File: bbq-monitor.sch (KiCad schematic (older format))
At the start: 51 parts, among them J1 Power, J2 USB_B_Mini, J3 Thermocouple, Q1 AO3401A, Q2 BC847, Q3 BC847, SW1 SW_Push, U1 ESP32-WROOM-32D, U2 TPS62132, U3 CP2104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

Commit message: up
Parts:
- removed C12, C14: 100n, Capacitor_SMD:C_0603_1608Metric, symbol Device:C_Small
- removed C13, C15: 10n, Capacitor_SMD:C_0603_1608Metric, symbol Device:C_Small
- removed C16: 100n, Capacitor_SMD:C_0402_1005Metric, symbol Device:C_Small
- removed C17: 10u, Capacitor_SMD:C_0402_1005Metric, symbol Device:C_Small
- removed H4: TR, MountingHole:MountingHole_3.2mm_M3_Pad_Via, symbol Mechanical:MountingHole
- removed U5: AD8495, Package_SO:MSOP-8_3x3mm_P0.65mm, symbol Sensor_Temperature:AD8495
- removed U6: DHT11, Sensor:Aosong_DHT11_5.5x12.0_P2.54mm, symbol Sensor:DHT11
- added C9: 100n, Capacitor_SMD:C_0603_1608Metric, symbol Device:C_Small
- added D3, D4, D5: RED, LED_SMD:LED_0603_1608Metric, symbol Device:LED_Small
- added D6: D_Zener, Diode_SMD:D_1206_3216Metric, symbol Device:D_Zener
- added D7: D_Schottky, Diode_SMD:D_1206_3216Metric, symbol Device:D_Schottky
- added IC1: MAX6675, hardware libraries:SO08, symbol MAX6675:MAX6675
- added Q4: AO3401A, Package_TO_SOT_SMD:SOT-23, symbol Transistor_FET:AO3401A
- J1: value Power -> Battery Power
- R10, R11, R9: value 1M -> 220; LCSC Part # C4190 -> (none)
- R13: value 100 -> 10k
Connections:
- net +3V3: now also C9.1, D3.2 (A), D4.2 (A), D5.2 (A), IC1.4 (VCC); no longer R12.1
- net +5V: now also R12.2, D7.2 (A), Q4.1 (G)
- net GND: now also J3.1 (Pin_1), R12.1, C9.2, IC1.1 (GND), IC1.2 (T-)
- net THERMO_SPI_CS: now reaches U1.29 (IO5)
- net THERMO_SPI_CS: now also IC1.6 (/CS)
- net THERMO_SPI_CLK: now reaches U1.30 (IO18)
- net THERMO_SPI_CLK: now also IC1.5 (SCK)
- net THERMO_SPI_DO: now reaches U1.31 (IO19)
- net THERMO_SPI_DO: now also IC1.7 (DO)
- net RX_LED: now reaches U3.13 (GPIO.1)
- net RX_LED: now also R11.1
- net TX_LED: now reaches U3.14 (GPIO.0)
- net TX_LED: now also R10.1
- net BATT_PWR: now reaches F1.2, J1.1 (Pin_1)
- net at Q1.1 (G), R13.2: now also D6.2 (A)
- net at J3.2 (Pin_2): now also IC1.3 (T+); no longer R10.1
- net BATT: no longer names the net of C1.1, C2.1, U2.10 (AVIN), U2.11 (PVIN), U2.12 (PVIN), U2.13 (EN)
- net BATT: now also D7.1 (K), Q4.2 (S); no longer Q1.2 (S), R14.1
- net TEMP_HUMID_SEN: no longer names the net of U1.6 (IO34)
- net TEMP_HUMID_SEN: no longer R12.2
- net THERMOCOUPLE: no longer names the net of U1.11 (IO26)
- net Thermocouple_INPUT_FILTERED+: no longer names the net of R10.2
- net Thermocouple_INPUT_FILTERED+: now also D4.1 (K)
- net Thermocouple_INPUT_FILTERED-: no longer names the net of R11.2
- net Thermocouple_INPUT_FILTERED-: now also D5.1 (K)
- new net: D3.1 (K), R9.2
- new net BATT_SAFE: D6.1 (K), Q1.2 (S), Q4.3 (D), R14.1
- no-connect marks 38 -> 35
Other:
- note added: "15V"
- note added: "LEDs\n"
- note added: "Schottky Value at Max Input Voltage"
- note added: "T+\n"
- note added: "T-\n"
- note removed: "Temperature and Humidity\n"
- moved on the sheet: C1, C10, C11, C2, C3, C4, C5, C6, C7, C8, D1, D2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

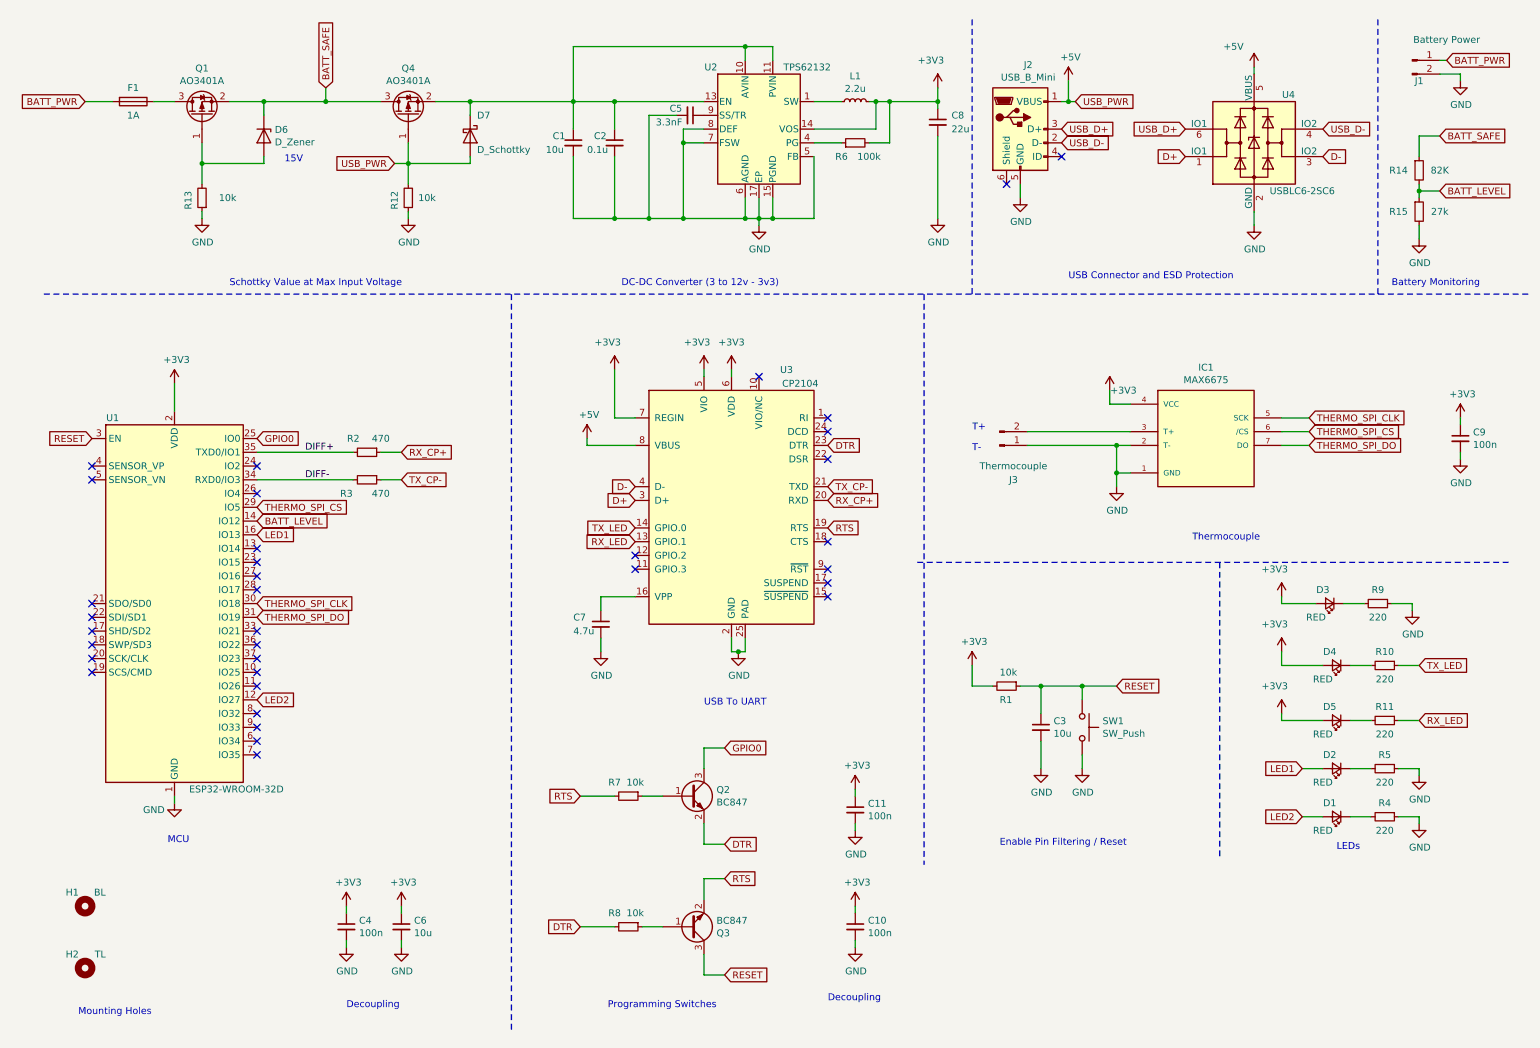
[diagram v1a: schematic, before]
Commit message: dc-dc is too expexpesnive - project is on hold
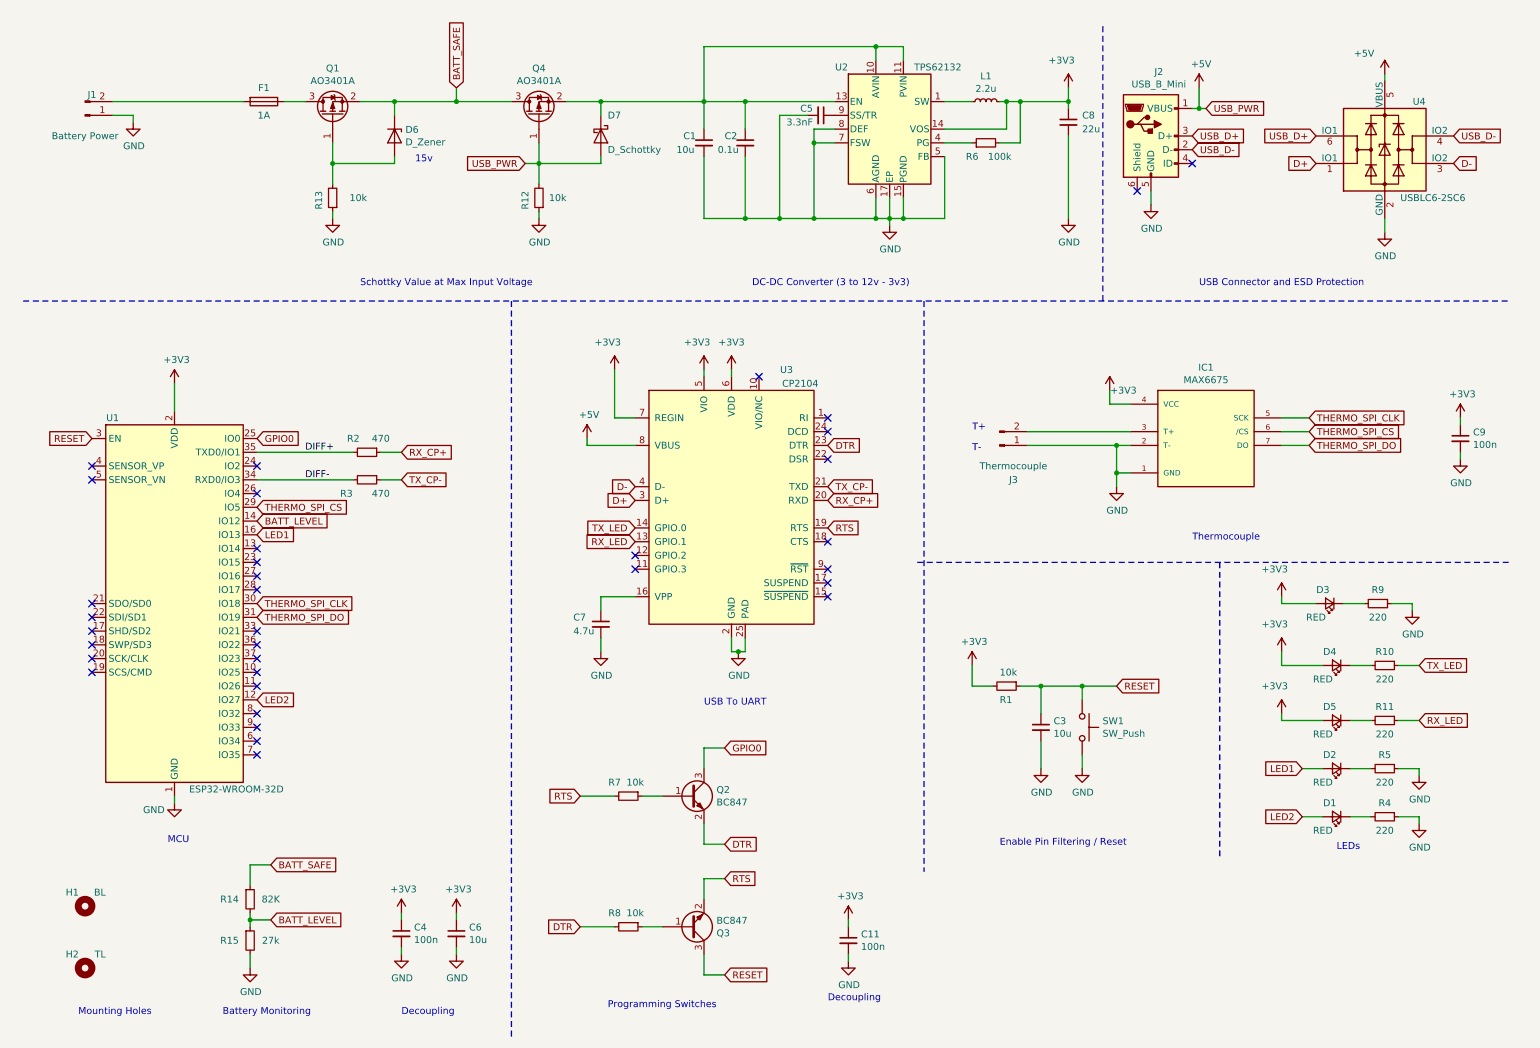
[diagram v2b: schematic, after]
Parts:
- removed C10: 100n, Capacitor_SMD:C_0603_1608Metric, symbol Device:C_Small
- C1, C3, C6: LCSC Part # (none) -> C96446
- C11, C4, C9: LCSC Part # (none) -> C14663
- D1, D2, D3, D4, D5: LCSC Part # (none) -> C2286
- H1, H2: footprint MountingHole:MountingHole_3.2mm_M3_Pad_Via -> MountingHole:MountingHole_3.2mm_M3
- J1, J3: footprint Connector_Molex:Molex_KK-254_AE-6410-02A_1x02_P2.54mm_Vertical -> rs-components:RS-Pro-5mm-Pitch-2-Pin-Terminal
- Q1, Q4: LCSC Part # (none) -> C15127
- Q2, Q3: LCSC Part # (none) -> C8664
- R1, R12, R13, R7, R8: LCSC Part # (none) -> C25804
- R10, R11, R4, R5, R9: LCSC Part # (none) -> C22962
- R2, R3: LCSC Part # (none) -> C23179
- U1: LCSC Part # (none) -> C473012
- U2: LCSC Part # (none) -> C81563
- U3: LCSC Part # (none) -> C47742 Copy
- U4: LCSC Part # (none) -> C2827654
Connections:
- net GND: now also J1.1 (Pin_1); no longer J1.2 (Pin_2)
- net BATT_PWR: no longer names the net of F1.2
- net BATT_PWR: now also J1.2 (Pin_2); no longer J1.1 (Pin_1)
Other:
- note added: "15v"
- note removed: "15V"
- moved on the sheet: C1, C11, C2, C4, C5, C6, C8, D6, D7, F1, J1, J2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
